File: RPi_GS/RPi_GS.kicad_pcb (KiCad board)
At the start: 2 copper layers, 65 x 56 mm, 12 parts, among them J1 PJ-202A, P1 Conn_02x20_Odd_Even, SW1 SW_Push_Open_Dual, U1 E32400M30S, U2 OLED

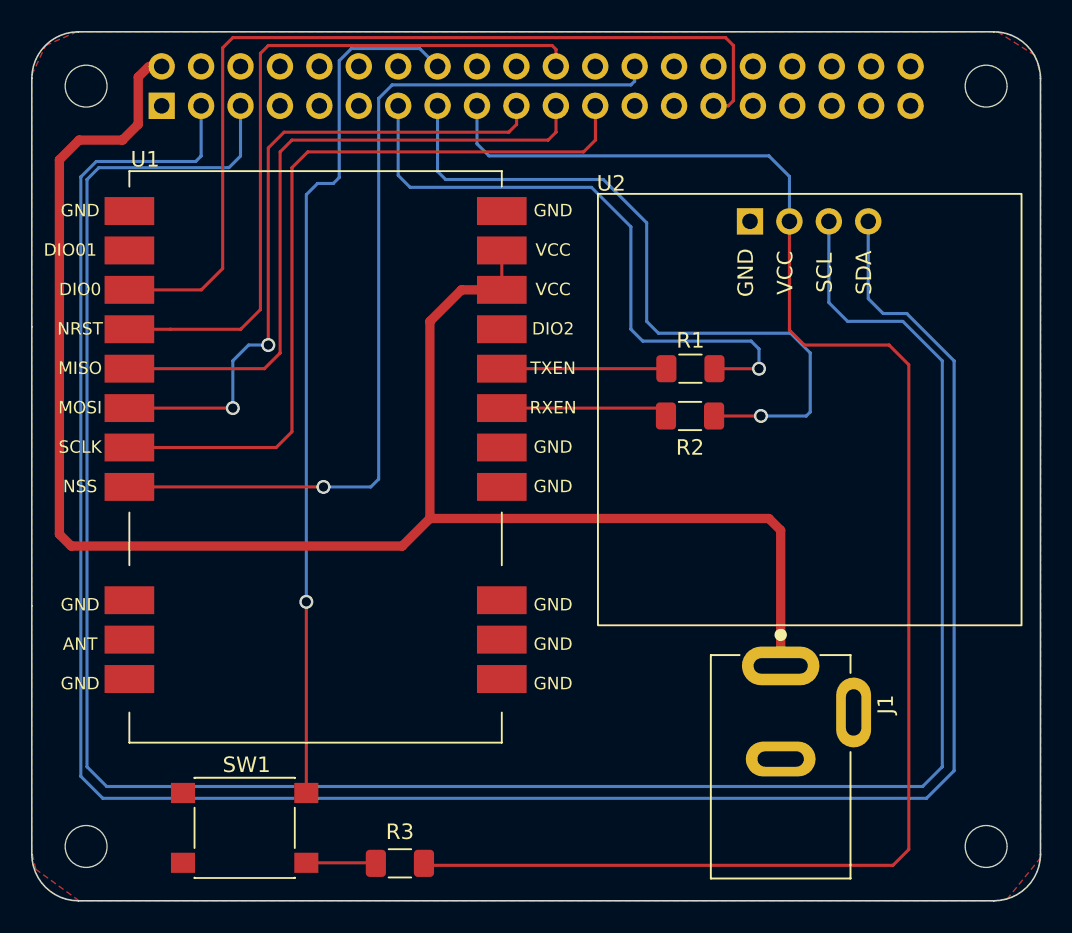
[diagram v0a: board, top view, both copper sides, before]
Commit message: Added test button, changed to smd for whatever I could, added power planes
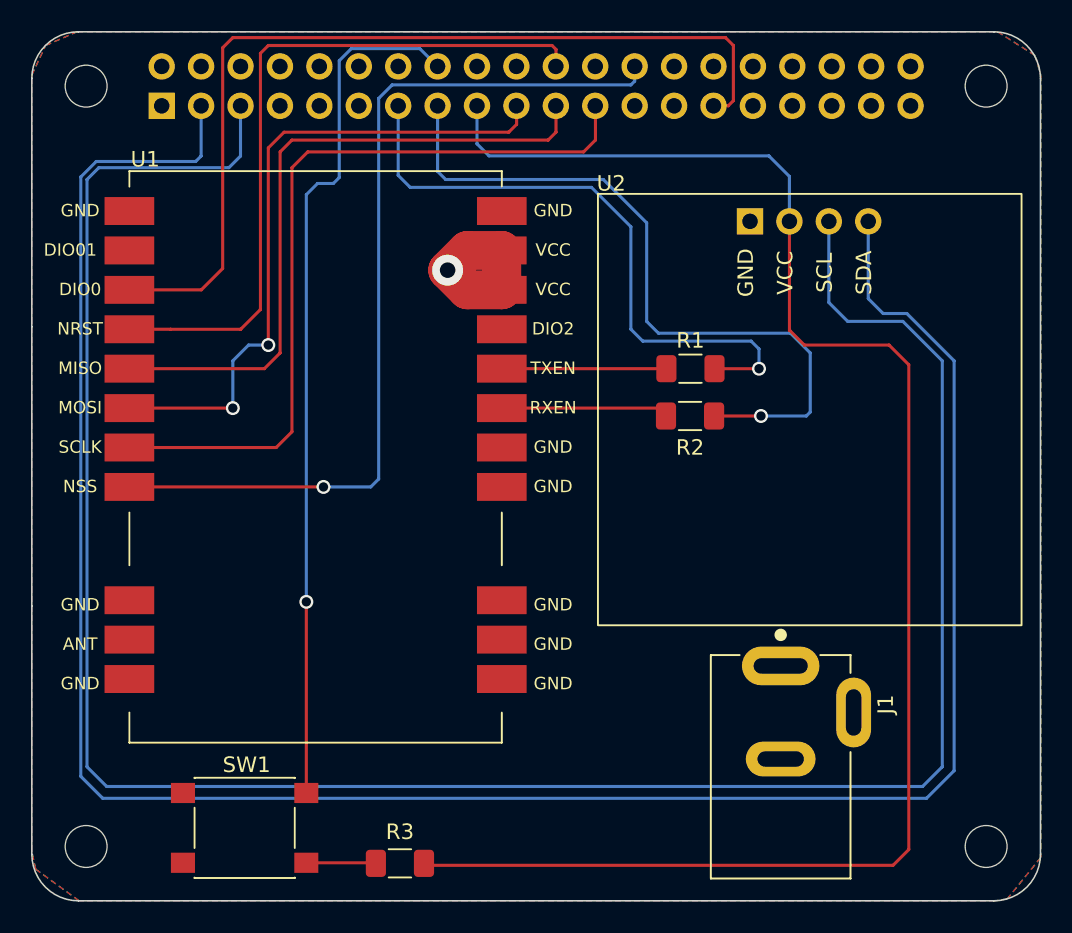
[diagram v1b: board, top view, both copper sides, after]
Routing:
- net +5V: track 112.3 -> 10.6 mm, vias 0 -> 1
- added copper zone on B.Cu, net +5V
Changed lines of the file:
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@@
   (segment (start 229.464 101.994) (end 247.498 101.994) (width 0.2) (layer "B.Cu") (net 1))
   (segment (start 228.69 101.22) (end 229.464 101.994) (width 0.2) (layer "B.Cu") (net 1))
-  (segment (start 248.26 126.124) (end 247.498 125.362) (width 0.6) (layer "F.Cu") (net 2))
-  (segment (start 230.288 110.629) (end 227.687 110.629) (width 0.6) (layer "F.Cu") (net 2))
-  (segment (start 201.778 102.248) (end 203.048 100.978) (width 0.6) (layer "F.Cu") (net 2))
-  (segment (start 223.876 127.14) (end 202.54 127.14) (width 0.6) (layer "F.Cu") (net 2))
-  (segment (start 201.778 126.378) (end 201.778 102.248) (width 0.6) (layer "F.Cu") (net 2))
-  (segment (start 205.842 100.978) (end 206.858 99.962) (width 0.6) (layer "F.Cu") (net 2))
-  (segment (start 247.498 125.362) (end 225.654 125.362) (width 0.6) (layer "F.Cu") (net 2))
-  (segment (start 202.54 127.14) (end 201.778 126.378) (width 0.6) (layer "F.Cu") (net 2))
-  (segment (start 227.687 110.629) (end 225.654 112.662) (width 0.6) (layer "F.Cu") (net 2))
-  (segment (start 225.654 112.662) (end 225.654 125.362) (width 0.6) (layer "F.Cu") (net 2))
-  (segment (start 206.858 99.962) (end 206.858 96.914) (width 0.6) (layer "F.Cu") (net 2))
-  (segment (start 203.048 100.978) (end 205.842 100.978) (width 0.6) (layer "F.Cu") (net 2))
-  (segment (start 230.288 108.089) (end 230.288 110.629) (width 0.2) (layer "F.Cu") (net 2))
-  (segment (start 206.858 96.914) (end 207.542 96.23) (width 0.6) (layer "F.Cu") (net 2))
-  (segment (start 225.654 125.362) (end 223.876 127.14) (width 0.6) (layer "F.Cu") (net 2))
-  (segment (start 207.542 96.23) (end 208.37 96.23) (width 0.2) (layer "F.Cu") (net 2))
-  (segment (start 248.26 134.864) (end 248.26 126.124) (width 0.6) (layer "F.Cu") (net 2))
+  (segment (start 226.797 109.36) (end 228.068 108.089) (width 2.5) (layer "F.Cu") (net 2))
+  (segment (start 230.288 108.089) (end 230.288 110.629) (width 2.5) (layer "F.Cu") (net 2))
+  (segment (start 228.066 110.629) (end 230.288 110.629) (width 2.5) (layer "F.Cu") (net 2))
+  (segment (start 226.797 109.36) (end 228.066 110.629) (width 2.5) (layer "F.Cu") (net 2))
+  (segment (start 228.068 108.089) (end 230.288 108.089) (width 2.5) (layer "F.Cu") (net 2))
+  (via (at 226.797 109.36) (size 2) (drill 1) (layers "F.Cu" "B.Cu") (free) (net 2))
   (segment (start 244.88 98.77) (end 243.93 98.77) (width 0.2) (layer "F.Cu") (net 6))
   (segment (start 210.922 110.63) (end 212.300489 109.251511) (width 0.2) (layer "F.Cu") (net 6))
@@
   (segment (start 230.288 115.709) (end 240.893 115.709) (width 0.2) (layer "F.Cu") (net 38))
   (zone (net 3) (net_name "GND") (layer "F.Cu") (hatch edge 0.508)
-    (connect_pads (clearance 0.508))
+    (connect_pads yes (clearance 0.508))
     (min_thickness 0.254) (filled_areas_thickness no)
     (fill yes (thermal_gap 0.508) (thermal_bridge_width 0.508))
+    (polygon
+      (pts
+        (xy 264.643 95.517)
+        (xy 265.024 96.787)
+        (xy 265.024 147.206)
+        (xy 262.865 149.873)
+        (xy 262.103 150)
+        (xy 203.048 150)
+        (xy 200.254 147.968)
+        (xy 200 146.825)
+        (xy 200 96.787)
+        (xy 200.889 94.882)
+        (xy 202.921 93.993)
+        (xy 262.23 93.993)
+      )
+    )
+  )
+  (zone (net 2) (net_name "+5V") (layer "B.Cu") (hatch edge 0.508)
+    (connect_pads yes (clearance 0.508))
+    (min_thickness 0.254) (filled_areas_thickness no)
+    (fill yes (thermal_gap 0.508) (thermal_bridge_width 0.508))
